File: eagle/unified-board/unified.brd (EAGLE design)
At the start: 203.2 x 101.6 mm, 286 parts, among them IC101 THAT151x, IC201 THAT151x, IC301 THAT151x, IC401 THAT151x, J103 phantom, J104 eqout, J105 eqout, J203 phantom, J204 eqout, J205 eqout, J303 phantom, J304 eqout, J305 eqout, J403 phantom, J404 eqout, J405 eqout, J501 out2, J601 out2, J701 power, U101 lme49710, U201 lme49710, U301 lme49710, U401 lme49710, U501 lme49710, U502 LM3915N, U601 lme49710, U602 LM3915N

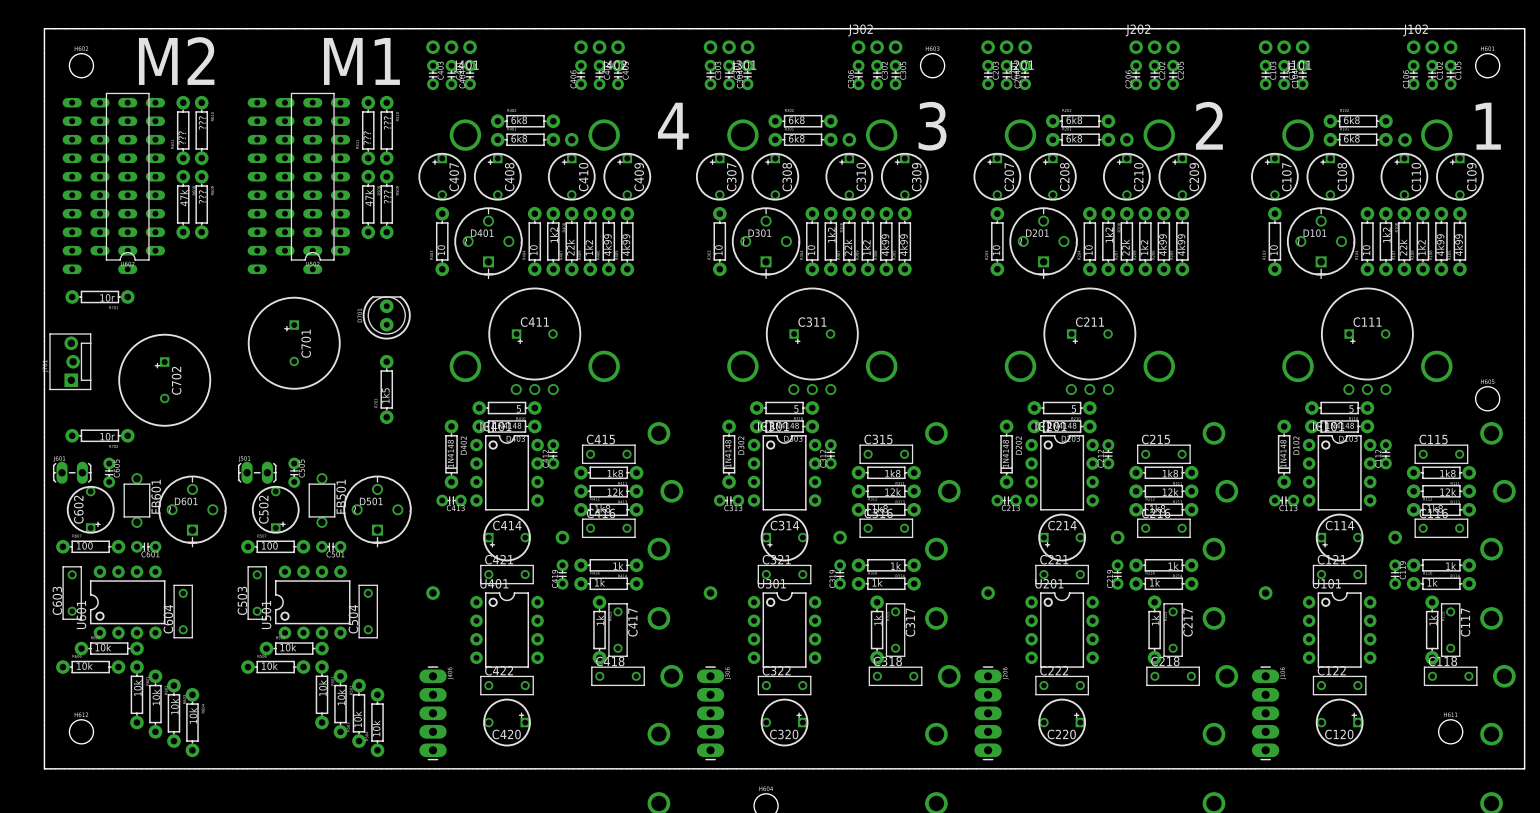
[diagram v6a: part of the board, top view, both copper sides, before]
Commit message: Channels routed...
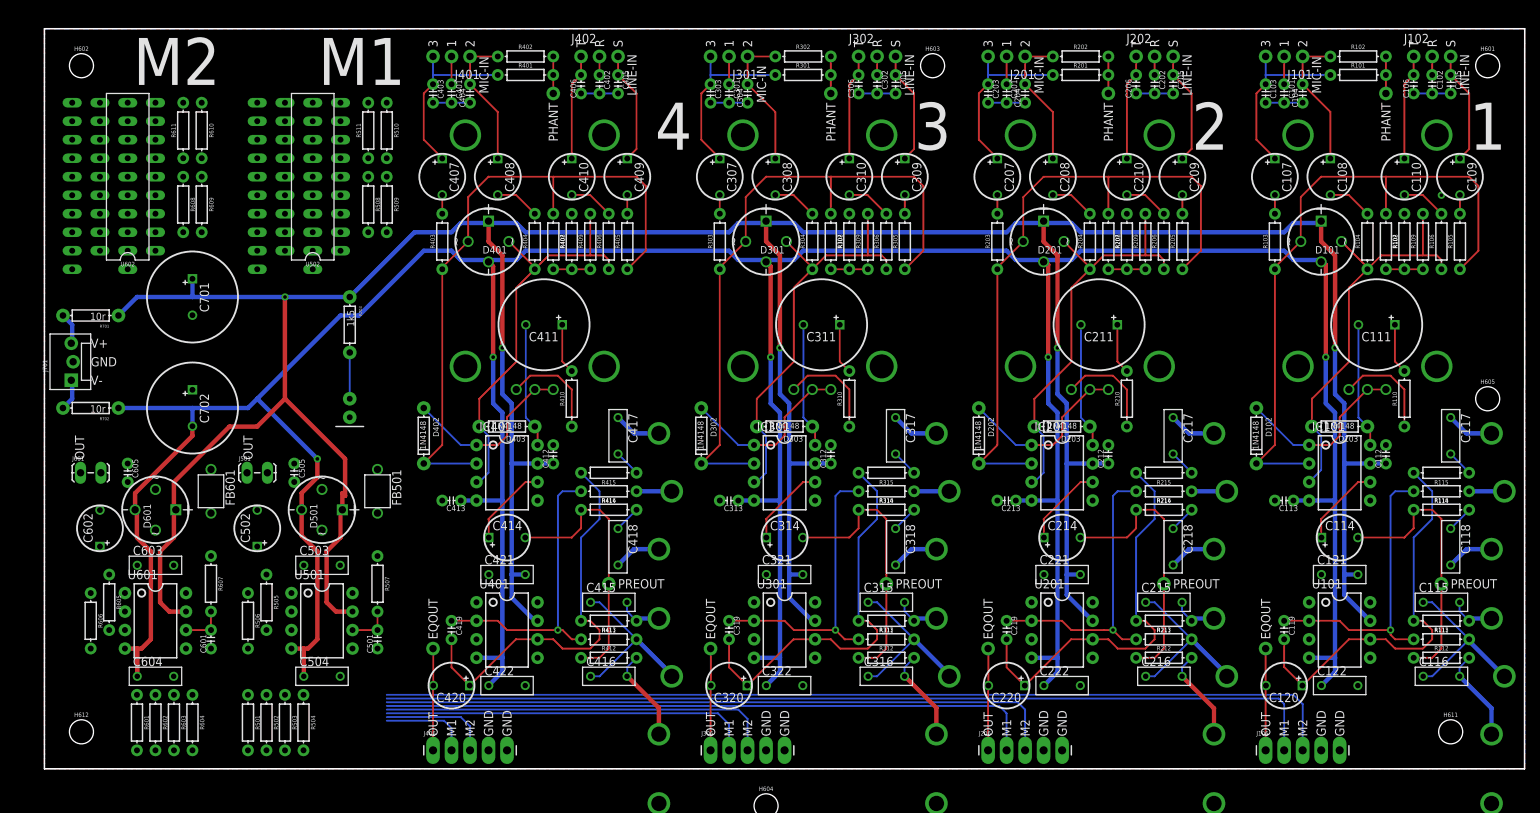
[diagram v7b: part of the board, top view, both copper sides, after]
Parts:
- R101, R102, R103, R104, R105, R106, R107, R108, R109, R110, R111, R112, R113, R114, R115, R116, R201, R202, R203, R204, R205, R206, R207, R208, R209, R210, R211, R212, R213, R214, R215, R216, R301, R302, R303, R304, R305, R306, R307, R308, R309, R310, R311, R312, R313, R314, R315, R316, R401, R402, R403, R404, R405, R406, R407, R408, R409, R410, R411, R412, R413, R414, R415, R416, R501, R502, R503, R504, R505, R506, R507, R508, R509, R510, R511, R601, R602, R603, R604, R605, R606, R607, R608, R609, R610, R611: device SparkFun-Resistors:AXIAL-0.3 -> mixer:AXIAL-0.3
- moved C117 26.7 mm to (193.0, 45.7)
- moved C217 26.7 mm to (154.9, 45.7)
- moved C317 26.7 mm to (116.8, 45.7)
- moved C417 26.7 mm to (78.7, 45.7)
- moved VR102 25.4 mm to (181.6, 12.7)
- moved VR103 25.4 mm to (181.6, 38.1)
- moved VR202 25.4 mm to (143.5, 12.7)
- moved VR203 25.4 mm to (143.5, 38.1)
- moved VR302 25.4 mm to (105.4, 12.7)
- moved VR303 25.4 mm to (105.4, 38.1)
- moved VR402 25.4 mm to (67.3, 12.7)
- moved VR403 25.4 mm to (67.3, 38.1)
- moved R115 21.6 mm to (191.8, 40.6), turned to 180 degrees
- moved R315 21.6 mm to (115.6, 40.6), turned to 180 degrees
- moved R415 21.6 mm to (77.5, 40.6), turned to 180 degrees
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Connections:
- net EQ1OUT1 renamed EQ2OUT
- net EQ1OUT2 renamed EQ3OUT
- net EQ1OUT3 renamed EQ4OUT
- net N$23 renamed M1GND
- net N$25 renamed M1-
- net N$26 renamed M1+
- net N$36 renamed L1GND
- net N$38 renamed L1-
- net N$39 renamed L1+
- net N$9 renamed PREOUT
- net N$114: now also D301.AC2; no longer D301.AC1
- net N$115: now also D301.AC1; no longer D301.AC2
- net N$146: now also D401.AC2; no longer D401.AC1
- net N$147: now also D401.AC1; no longer D401.AC2
- net N$30: now also D101.AC2; no longer D101.AC1
- net N$31: now also D101.AC1; no longer D101.AC2
- net N$82: now also D201.AC2; no longer D201.AC1
- net N$83: now also D201.AC1; no longer D201.AC2
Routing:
- net VNEG: track 0.00 -> 544.7 mm, vias 0 -> 5
- net VCC: track 0.00 -> 531.6 mm, vias 0 -> 5
- net 1TO2: track 0.00 -> 132.6 mm
- net 1TO1: track 0.00 -> 129.9 mm
- net 2TO2: track 0.00 -> 93.6 mm
- net 2TO1: track 0.00 -> 90.6 mm
- net N$114: track 0.00 -> 90.0 mm
- net N$30: track 0.00 -> 90.0 mm
- net N$146: track 0.00 -> 90.0 mm
- net N$82: track 0.00 -> 90.0 mm
- net N$83: track 0.00 -> 57.3 mm
- net N$147: track 0.00 -> 57.3 mm
- net N$115: track 0.00 -> 57.3 mm
- net N$31: track 0.00 -> 57.0 mm
- net N$148: track 0.00 -> 55.6 mm
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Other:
- board text added: "EQOUT"
- board text added: "GND"
- board text added: "LINE-IN"
- board text added: "MIC-IN"
- board text added: "OUT"
- board text added: "PHANT"
- board text added: "PREOUT"
- board text added: "R"
- board text added: "S"
- board text added: "T"
- board text added: "V+"
- board text added: "V-"

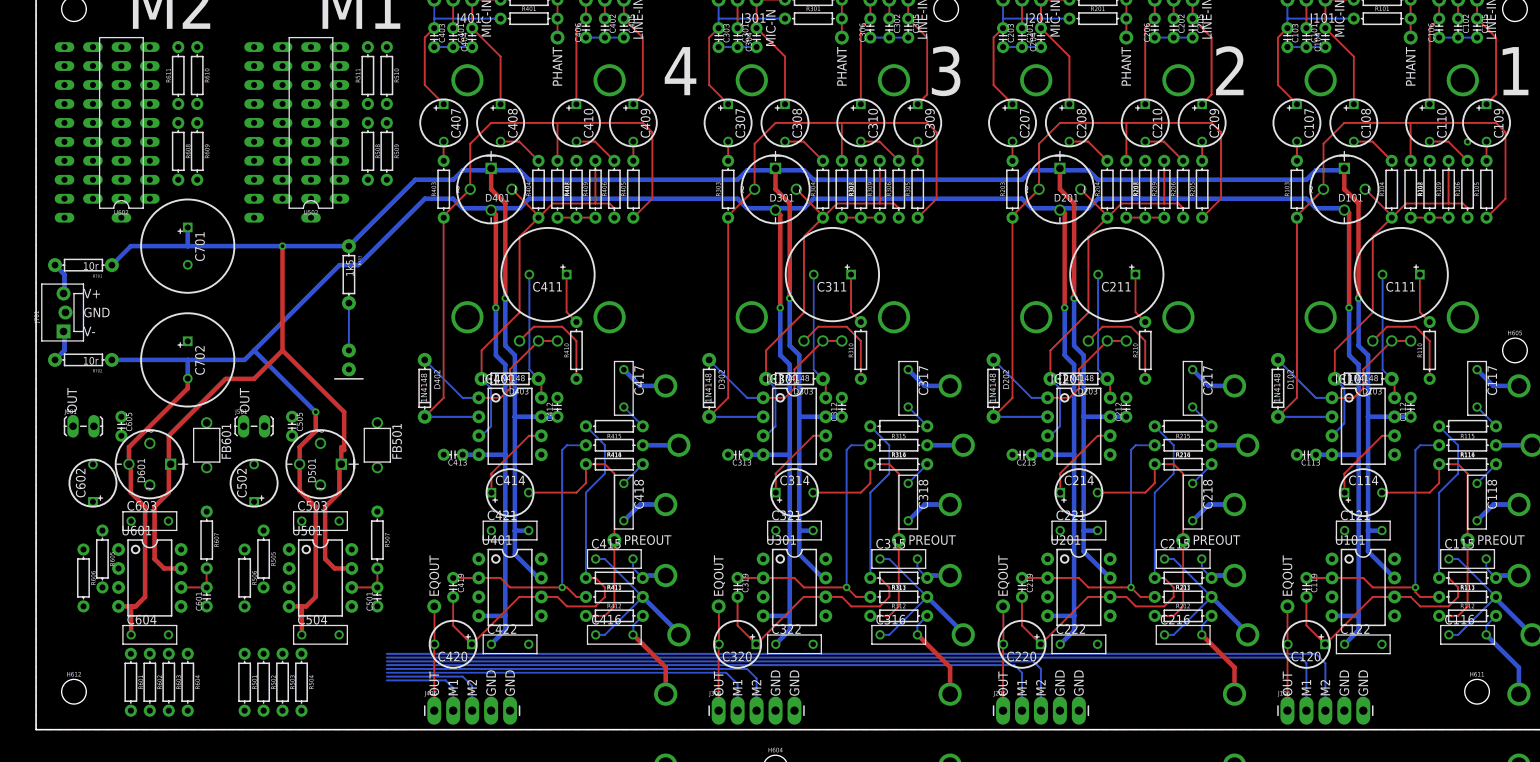
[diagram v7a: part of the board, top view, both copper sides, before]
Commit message: Keeping moving.
Calculated preamp R-strings.
Tried for the bargraphs...jusy is still out...
Added peak tracker for meter circuit.
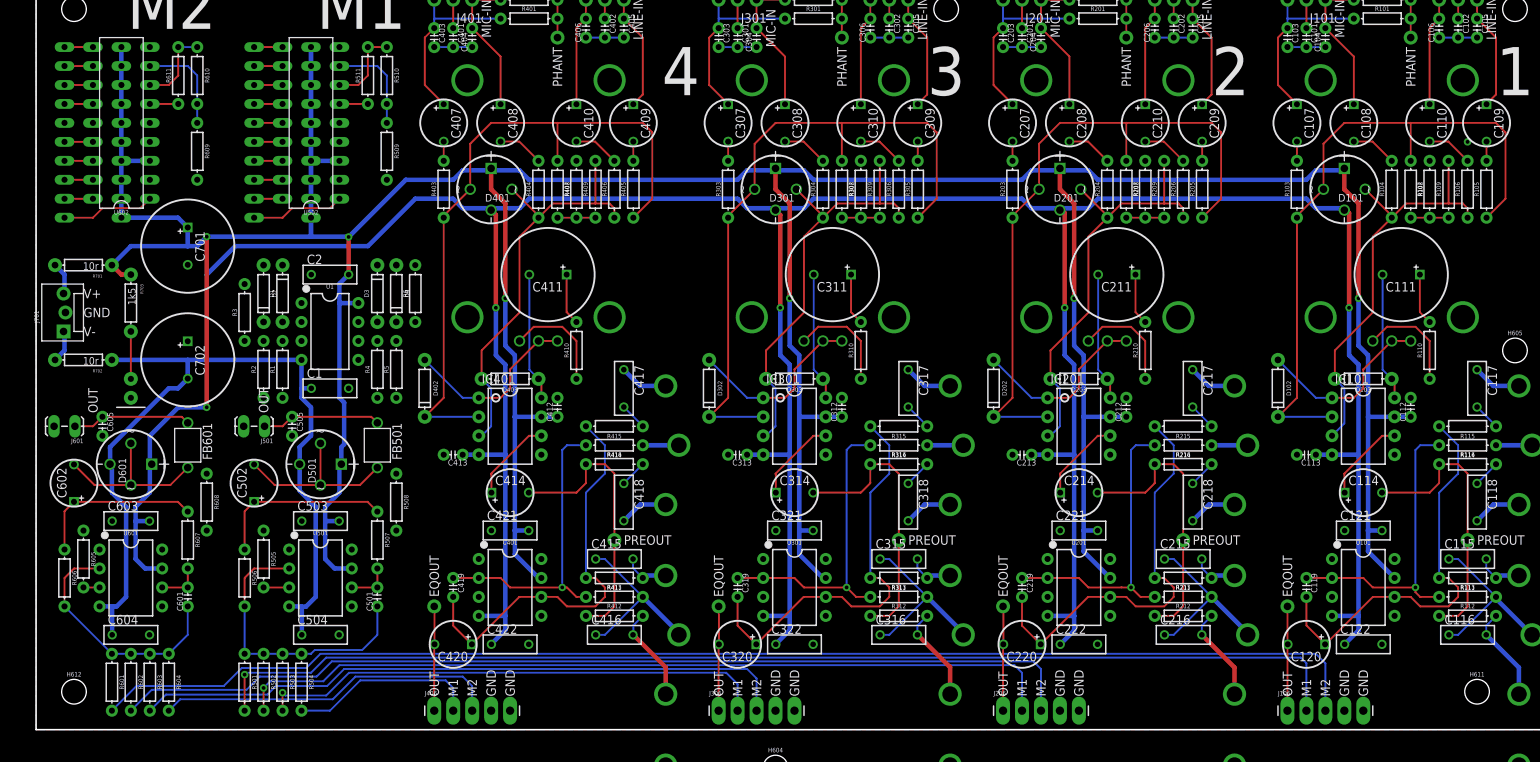
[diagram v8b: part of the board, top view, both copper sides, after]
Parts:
- added C1, C2: 0.01uf, mixer:WIMA-MKS2-2.5X7.2
- added D1, D2, D3, D4: 1n4148, SparkFun-DiscreteSemi:DIODE-1N4148
- added R1, R4: 10k, mixer:AXIAL-0.3
- added R2, R5: 100k, mixer:AXIAL-0.3
- added R3, R6: 1k, mixer:AXIAL-0.3
- added U1: LM358, mixer:DIP08
- D102, D103, D202, D203, D302, D303, D402, D403: value 1N4148 -> 200mA/100V/1V
- moved R508 47.1 mm to (48.3, 30.5)
- moved R608 47.1 mm to (22.9, 30.5)
- moved D701 29.5 mm to (12.7, 45.7)
- moved R703 29.5 mm to (12.7, 57.1)
- moved C603 2.54 mm to (12.7, 27.9)
- moved C604 2.54 mm to (12.7, 12.7)
- moved D601 2.54 mm to (12.7, 35.6)
- moved R602 2.54 mm to (12.7, 6.35)
- moved R603 2.54 mm to (15.2, 6.35)
- moved R605 2.54 mm to (6.35, 22.9)
- moved U601 2.54 mm to (12.7, 20.3)
- moved C602 2.54 mm to (5.08, 33.0)
- moved R606 2.54 mm to (3.81, 20.3)
- moved C601 2.54 mm to (20.3, 17.8)
- moved C605 2.54 mm to (8.89, 40.6)
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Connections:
- new net N$18: D2.C, R2.P$2, R3.P$1
- new net N$23: R3.P$2, U602.5
- new net N$25: D3.A, R4.P$2, R5.P$1, U1.6
- new net N$26: D3.C, D4.A, U1.7
- new net N$36: D4.C, R5.P$2, R6.P$1
- new net N$5: D1.A, R1.P$2, R2.P$1, U1.2
- new net N$9: D1.C, D2.A, U1.1
- net GND: now also C1.P$1, C2.P$2, U1.3, U1.5
- net N$11: now also R1.P$1; no longer U602.5
- net VCC: now also C2.P$1, U1.8
- net VNEG: now also C1.P$2, U1.4
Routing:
- net VCC: track 531.6 -> 616.1 mm, vias 5 -> 7
- net 1TO2: track 132.6 -> 172.6 mm
- net N$150: track 0.00 -> 39.3 mm
- net 2TO2: track 93.6 -> 130.7 mm
- net 3TO2: track 54.4 -> 88.4 mm
- net N$17: track 0.00 -> 33.0 mm
- net 4TO2: track 15.3 -> 46.4 mm
- net 1TO1: track 129.9 -> 154.7 mm, vias 0 -> 1
- net N$152: track 0.00 -> 24.2 mm
- net N$164: track 0.00 -> 24.0 mm
- net N$11: track 0.00 -> 22.9 mm
- net N$12: track 0.00 -> 22.7 mm
- net 2TO1: track 90.6 -> 111.4 mm, vias 0 -> 1
- net VNEG: track 544.7 -> 562.8 mm, vias 5 -> 4
- net 3TO1: track 51.2 -> 69.0 mm, vias 0 -> 1
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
